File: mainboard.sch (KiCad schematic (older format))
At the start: 35 parts, among them J1 105017-1001, J2 Conn_01x04_Female, J3 Conn_01x02_Female, J4 Conn_01x09_Female, J5 Conn_01x02_Female, J6 Conn_01x02_Female, J7 Conn_01x04_Female, J8 Conn_01x03_Female, Q1 AOD4184A, U1 ESP32-WROOM-32E_(16MB)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

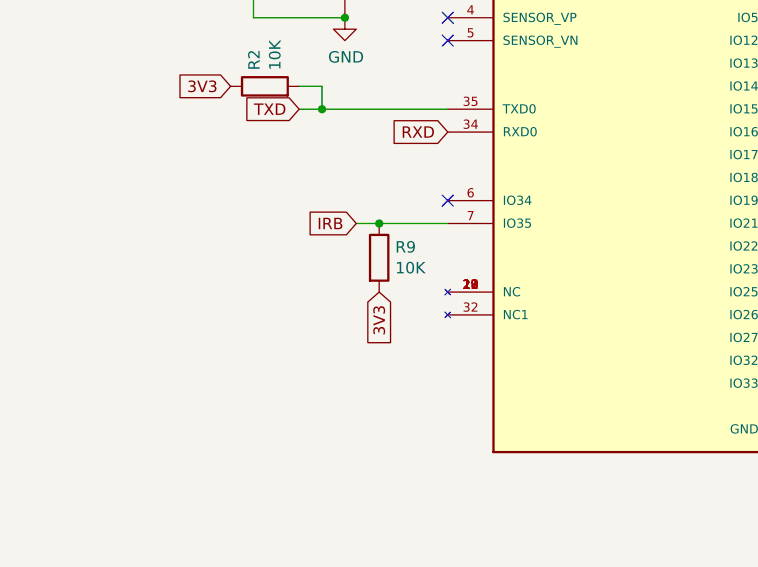
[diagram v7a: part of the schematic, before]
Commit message: fixes
10k pullup
mute aan 5V
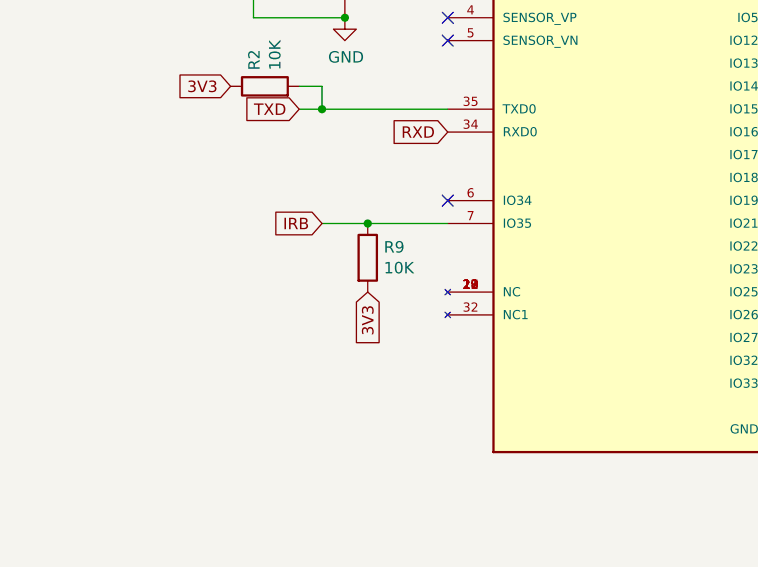
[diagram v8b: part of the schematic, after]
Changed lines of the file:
@@
 Wire Wire Line
 	7895 3555 8045 3555
-Text GLabel 1950 3150 0    50   Input ~ 0
+Text GLabel 1800 3150 0    50   Input ~ 0
 IRB
 Text GLabel 3950 2150 2    50   Input ~ 0
@@
 $Comp
 L Device:R R9
-U 1 1 606A03C4
-P 2050 3300
-F 0 "R9" H 2120 3346 50  0000 L CNN
-F 1 "10K" H 2120 3255 50  0000 L CNN
-F 2 "Resistor_SMD:R_0805_2012Metric_Pad1.20x1.40mm_HandSolder" V 1980 3300 50  0001 C CNN
-F 3 "~" H 2050 3300 50  0001 C CNN
-	1    2050 3300
-	1    0    0    -1
-$EndComp
-Wire Wire Line
-	1950 3150 2050 3150
-Wire Wire Line
-	2050 3150 2350 3150
-Connection ~ 2050 3150
-Text GLabel 2050 3450 3    50   Input ~ 0
+U 1 1 606C98CA
+P 2000 3300
+F 0 "R9" H 2070 3346 50  0000 L CNN
+F 1 "10K" H 2070 3255 50  0000 L CNN
+F 2 "Resistor_SMD:R_0805_2012Metric_Pad1.20x1.40mm_HandSolder" V 1930 3300 50  0001 C CNN
+F 3 "~" H 2000 3300 50  0001 C CNN
+	1    2000 3300
+	1    0    0    -1
+$EndComp
+Wire Wire Line
+	2350 3150 2000 3150
+Connection ~ 2000 3150
+Wire Wire Line
+	2000 3150 1800 3150
+Text GLabel 2000 3450 3    50   Input ~ 0
 3V3
 Text GLabel 2700 6400 0    50   Input ~ 0
